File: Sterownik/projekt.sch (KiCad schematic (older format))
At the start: 73 parts, among them P3 CONN_01X05, P4 CONN_01X02, P5 CONN_01X02, P6 USB_OTG, P7 CONN_01X12, P8 CONN_01X02, SW1 SW_PUSH_SMALL, T1 Si2323DS, T10 Si2323DS, T12 2N7002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

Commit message: Additional changes
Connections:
- wire segments 280 -> 279
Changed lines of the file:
@@
 NoConn ~ 1750 3300
 NoConn ~ 6350 4300
-Text GLabel 10500 1250 0    39   Input ~ 0
-VUSB_BUS
 $Comp
 L C C20
@@
 	1700 6250 2900 6250
 Wire Wire Line
-	1500 6250 1600 6250
-Wire Wire Line
 	1500 6550 1600 6550
 Wire Wire Line
@@
 Wire Wire Line
 	1100 6350 1600 6350
-Connection ~ 1600 6250
 Wire Wire Line
 	5500 8350 5500 8400
@@
 	0    1    1    0
 $EndComp
-Text GLabel 10700 5100 0    39   Input ~ 0
-VUSB_BUS
 $Comp
 L 2N7002 T3
@@
 	1    0    0    -1
 $EndComp
-Text GLabel 10100 4300 1    39   Input ~ 0
-VUSB_BUS
 $Comp
 L R R5
@@
 	1150 6300 1150 6350
 Connection ~ 1150 6350
+Text GLabel 10700 5100 0    39   Input ~ 0
+VBUS
+Text GLabel 10500 1250 0    39   Input ~ 0
+VBUS
+Text GLabel 10100 4300 1    39   Input ~ 0
+VBUS
 $EndSCHEMATC

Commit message: 100% driver PCB routed - waiting for fixes
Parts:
- removed C20, C39, C40, C41: 100N, Capacitors_SMD:C_0603_HandSoldering, symbol C
- removed C23: 100U, SMD_Packages:SMD-1206_Pol, symbol CP
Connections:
- wire segments 279 -> 261

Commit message: Fixes commit.
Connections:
- net labels added: POWER_LED
- wire segments 261 -> 262
- no-connect marks 21 -> 20
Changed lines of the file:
@@
 	1    0    0    -1
 $EndComp
-Text GLabel 7950 4900 0    39   Input ~ 0
-MAINTAIN
 $Comp
 L R R19
@@
 	1    0    0    -1
 $EndComp
-NoConn ~ 6350 3300
 $Comp
 L dsPIC33EP256MU806 U2
@@
 	1700 3500 1750 3500
 NoConn ~ 1750 4000
+Text GLabel 6400 3300 2    39   Input ~ 0
+POWER_LED
+Wire Wire Line
+	6400 3300 6350 3300
+Text GLabel 7950 4900 0    39   Input ~ 0
+POWER_LED
 $EndSCHEMATC

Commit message: More fixes
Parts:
- C4: footprint Capacitors_Tantalum_SMD:TantalC_SizeX_EIA-7343 -> Footprinty:TantalC_SizeA_EIA-3216_HandSoldering
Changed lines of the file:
@@
 F 0 "C4" H 3175 8450 50  0000 L CNN
 F 1 "4,7u" H 3175 8250 50  0000 L CNN
-F 2 "Capacitors_Tantalum_SMD:TantalC_SizeX_EIA-7343" H 3188 8200 30  0001 C CNN
+F 2 "Footprinty:TantalC_SizeA_EIA-3216_HandSoldering" H 3188 8200 30  0001 C CNN
 F 3 "" H 3150 8350 60  0000 C CNN
 	1    3150 8350

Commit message: Simplifiying all
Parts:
- removed R32, R35, R5: 100K, Resistors_SMD:R_0603, symbol R
- removed T1: Si2323DS, Footprinty:SOT23, symbol Si2323DS
- removed T15, T3: 2N7002, Footprinty:2N7002-SOT23, symbol 2N7002
- removed T17: NTD25P03L, SMD_Packages:DPAK-3_GDS, symbol NTD25P03L
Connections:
- wire segments 262 -> 246
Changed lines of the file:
@@
 L VDD #PWR027
 U 1 1 559D16BE
-P 11650 8700
-F 0 "#PWR027" H 11650 8550 50  0001 C CNN
-F 1 "VDD" H 11650 8850 50  0000 C CNN
-F 2 "" H 11650 8700 60  0000 C CNN
-F 3 "" H 11650 8700 60  0000 C CNN
-	1    11650 8700
-	1    0    0    -1
-$EndComp
-Text GLabel 11700 8450 0    39   Input ~ 0
-MEM_ENABLE
-$Comp
-L R R32
-U 1 1 559D16CB
-P 11900 8450
-F 0 "R32" V 11980 8450 50  0000 C CNN
-F 1 "100K" V 11900 8450 50  0000 C CNN
-F 2 "Resistors_SMD:R_0603" V 11830 8450 30  0001 C CNN
-F 3 "" H 11900 8450 30  0000 C CNN
-	1    11900 8450
-	0    1    1    0
+P 12400 8550
+F 0 "#PWR027" H 12400 8400 50  0001 C CNN
+F 1 "VDD" H 12400 8700 50  0000 C CNN
+F 2 "" H 12400 8550 60  0000 C CNN
+F 3 "" H 12400 8550 60  0000 C CNN
+	1    12400 8550
+	1    0    0    -1
 $EndComp
 Text GLabel 1700 3500 0    39   Input ~ 0
@@
 Pamięć
 $Comp
-L 2N7002 T15
-U 1 1 5599A001
-P 12100 8750
-F 0 "T15" H 11950 8900 39  0000 C CNN
-F 1 "2N7002" V 12150 8750 39  0000 C CNN
-F 2 "Footprinty:2N7002-SOT23" H 12100 8750 39  0001 C CNN
-F 3 "" H 12100 8750 39  0000 C CNN
-	1    12100 8750
-	0    1    1    0
-$EndComp
-$Comp
-L NTD25P03L T17
-U 1 1 5599AA92
-P 13150 1050
-F 0 "T17" H 13000 1200 39  0000 C CNN
-F 1 "NTD25P03L" V 13250 1050 39  0000 C CNN
-F 2 "SMD_Packages:DPAK-3_GDS" H 13150 1050 39  0001 C CNN
-F 3 "" H 13150 1050 39  0000 C CNN
-	1    13150 1050
-	0    1    -1   0
-$EndComp
-$Comp
-L R R35
-U 1 1 5599CA4F
-P 13150 1450
-F 0 "R35" V 13230 1450 50  0000 C CNN
-F 1 "100K" V 13150 1450 50  0000 C CNN
-F 2 "Resistors_SMD:R_0603" V 13080 1450 30  0001 C CNN
-F 3 "" H 13150 1450 30  0000 C CNN
-	1    13150 1450
-	1    0    0    -1
-$EndComp
-$Comp
 L VDD #PWR033
 U 1 1 5599DAC5
@@
 $EndComp
 Text GLabel 6400 3200 2    39   Input ~ 0
-COMM_ENABLE
-Text GLabel 13150 1650 3    39   Input ~ 0
 COMM_ENABLE
 $Comp
@@
 	6350 2400 6400 2400
 Wire Wire Line
-	13150 1600 13150 1650
-Wire Wire Line
-	12850 1050 12950 1050
+	12850 1050 13900 1050
 Wire Wire Line
 	12850 1000 12850 1050
-Wire Wire Line
-	13150 1250 13150 1300
 Wire Wire Line
 	10900 5650 11100 5650
@@
 Wire Wire Line
 	12300 5100 12900 5100
-Wire Wire Line
-	10700 5100 10750 5100
 Wire Wire Line
 	6400 2300 6350 2300
@@
 	11600 5300 11600 5900
 Wire Wire Line
-	12050 8450 12100 8450
-Wire Wire Line
-	11750 8450 11700 8450
-Wire Wire Line
-	11900 8750 11650 8750
-Wire Wire Line
-	11650 8750 11650 8700
-Wire Wire Line
-	12100 8450 12100 8550
-Wire Wire Line
-	12300 8750 12400 8750
-Wire Wire Line
-	12400 8600 12400 8850
+	12400 8550 12400 8850
 Wire Wire Line
 	12400 8600 13150 8600
-Connection ~ 12400 8750
 Wire Wire Line
 	12400 9150 12250 9150
@@
 Wire Notes Line
 	14900 600  14900 3400
-Wire Wire Line
-	13350 1050 13900 1050
 Connection ~ 13400 1050
 Wire Wire Line
@@
 Wire Wire Line
 	5500 8350 5500 8400
-Text GLabel 9850 4950 0    39   Input ~ 0
-CHARGE_SIGNAL
-Wire Wire Line
-	10950 4700 10950 4900
-$Comp
-L Si2323DS T1
-U 1 1 559AC904
-P 10950 5100
-F 0 "T1" H 10800 5250 39  0000 C CNN
-F 1 "Si2323DS" V 11000 5100 39  0000 C CNN
-F 2 "Footprinty:SOT23" H 10950 5100 39  0001 C CNN
-F 3 "" H 10950 5100 39  0000 C CNN
-	1    10950 5100
-	0    1    1    0
-$EndComp
-$Comp
-L 2N7002 T3
-U 1 1 55A9E0B5
-P 10100 4950
-F 0 "T3" H 9950 5100 39  0000 C CNN
-F 1 "2N7002" V 10150 4950 39  0000 C CNN
-F 2 "Footprinty:2N7002-SOT23" H 10100 4950 39  0001 C CNN
-F 3 "" H 10100 4950 39  0000 C CNN
-	1    10100 4950
-	1    0    0    -1
-$EndComp
-$Comp
-L R R5
-U 1 1 55A9EFC2
-P 10100 4500
-F 0 "R5" V 10180 4500 50  0000 C CNN
-F 1 "100K" V 10100 4500 50  0000 C CNN
-F 2 "Resistors_SMD:R_0603" V 10030 4500 30  0001 C CNN
-F 3 "" H 10100 4500 30  0000 C CNN
-	1    10100 4500
-	1    0    0    -1
-$EndComp
-Wire Wire Line
-	10100 4650 10100 4750
-Wire Wire Line
-	10100 4300 10100 4350
-Wire Wire Line
-	10100 4700 10950 4700
-Connection ~ 10100 4700
-$Comp
-L GND #PWR055
-U 1 1 55AA0456
-P 10100 5900
-F 0 "#PWR055" H 10100 5650 50  0001 C CNN
-F 1 "GND" H 10100 5750 50  0000 C CNN
-F 2 "" H 10100 5900 60  0000 C CNN
-F 3 "" H 10100 5900 60  0000 C CNN
-	1    10100 5900
-	1    0    0    -1
-$EndComp
-Wire Wire Line
-	10100 5900 10100 5150
-Wire Wire Line
-	9900 4950 9850 4950
 $Comp
 L ZHCS1000 D1
@@
 Wire Wire Line
 	6350 3600 6400 3600
-Text GLabel 10700 5100 0    39   Input ~ 0
-VBUS
-Text GLabel 10100 4300 1    39   Input ~ 0
+Text GLabel 11150 5100 0    39   Input ~ 0
 VBUS
 $Comp
@@
 Text GLabel 7950 4900 0    39   Input ~ 0
 POWER_LED
+Connection ~ 12400 8600
 $EndSCHEMATC

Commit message: Simplier version - first fixes
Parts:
- removed P7: CONN_01X12, Footprinty:DS1065-02-1-12S8BS, symbol CONN_01X12
- added P1: CONN_01X08, Footprinty:DS1065-02-1X8S8BS, symbol CONN_01X08
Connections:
- net ADCDATA: now also P1.4 (P4)
- net CLOCK: now also P1.3 (P3)
- net GND: now also P1.8 (P8)
- net MAIN_VOL: now also P1.1 (P1)
- net SCL: now also P1.7 (P7)
- net SDA: now also P1.6 (P6)
- net SUSPEND: now also P1.5 (P5)
- net VDD: now also P1.2 (P2)
- net CLOCK_ENABLE: no longer names the net of U2.64 (AN28/PWM3L/PMD4/RP84/RE4)
- net COMM_ENABLE: no longer names the net of U2.46 (INT0/DMH/RP64/RD0)
- net CONV_ENABLE: no longer names the net of U2.5 (C1IN1-/SDI2/PMA4/RPI119/RG7)
- net HUM_ENABLE: no longer names the net of U2.1 (AN29/PWM3H/PMD5/RP85/RE5)
- net MEM_ENABLE: no longer names the net of U2.27 (TCK/AN12/PMA11/RPI44/RB12)
- net PRESS_ENABLE: no longer names the net of U2.63 (AN27/PWM2H/PMD3/RPI83/RE3)
- net SOUND_ENABLE: no longer names the net of U2.6 (C2IN3-/SDO2/PMA3/RP120/RG8)
- no-connect marks 20 -> 27

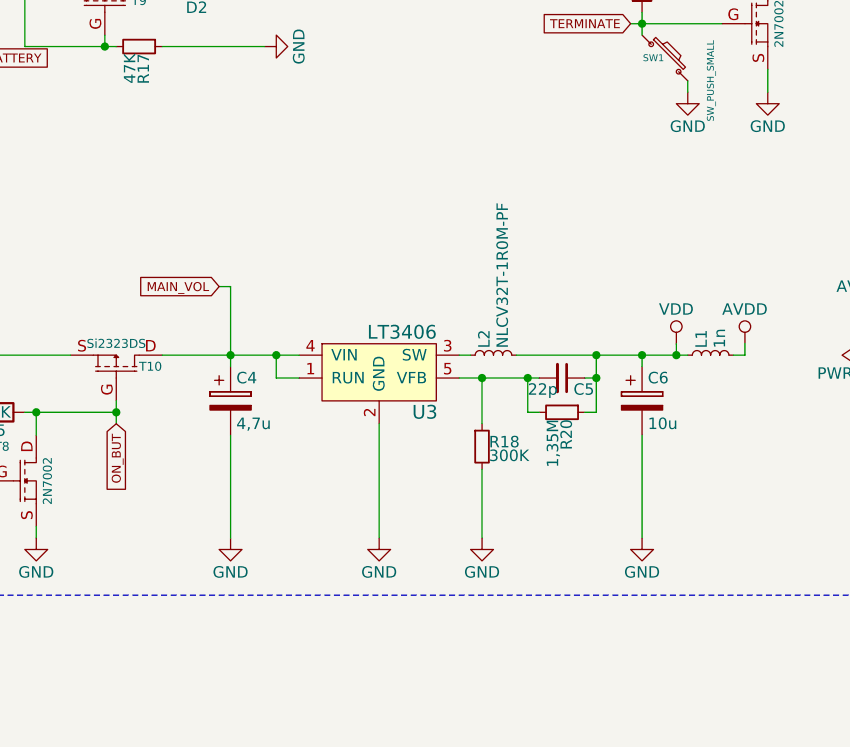
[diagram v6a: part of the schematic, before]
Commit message: DC/DC converter to linear converter change
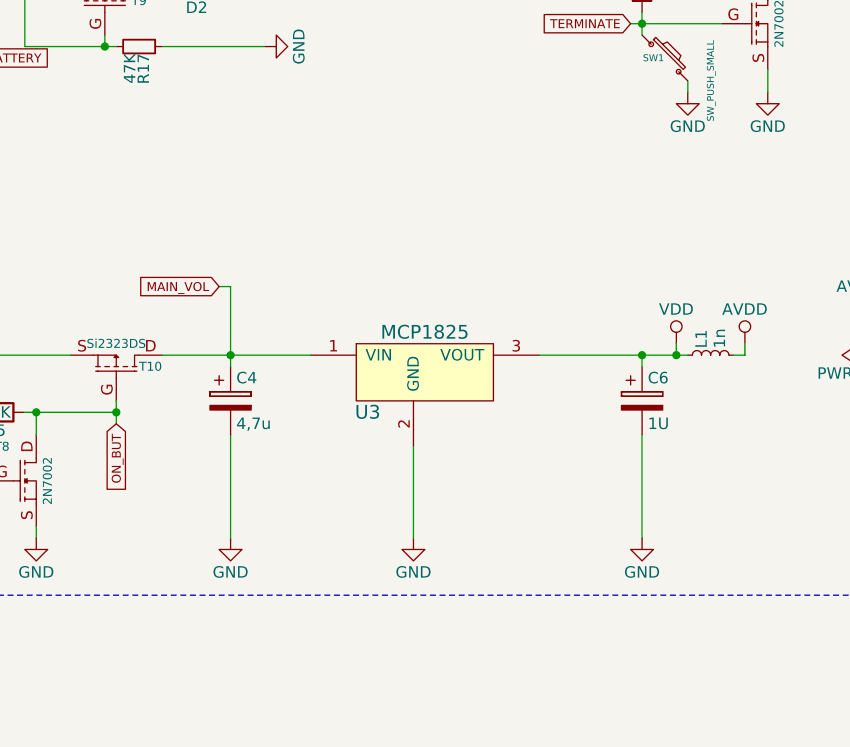
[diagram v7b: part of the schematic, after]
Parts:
- removed C5: 22p, Capacitors_SMD:C_0603, symbol C_Small
- removed L2: NLCV32T-1R0M-PF, Capacitors_SMD:C_1210, symbol L_Small
- removed R18: 300K, Resistors_SMD:R_0603, symbol R_Small
- removed R20: 1,35M, Resistors_SMD:R_0603, symbol R_Small
- removed U3: LT3406, Housings_SOT-23_SOT-143_TSOT-6:SOT-23-5, symbol LT3406
- added U3: MCP1825, SMD_Packages:SOT-223, symbol MCP1825
- C6: value 10u -> 1U; footprint Capacitors_Tantalum_SMD:TantalC_SizeB_EIA-3528_HandSoldering -> Capacitors_SMD:C_2220_HandSoldering
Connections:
- net GND: now also U3.2 (GND)
- net MAIN_VOL: now also U3.1 (VIN)
- net VDD: now also U3.3 (VOUT)
